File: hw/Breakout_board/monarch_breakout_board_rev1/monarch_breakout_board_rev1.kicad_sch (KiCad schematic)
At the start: 21 parts, among them U2 FDC2214RGHR, U3 INA226AQDGSRQ1, U4 INA226AQDGSRQ1

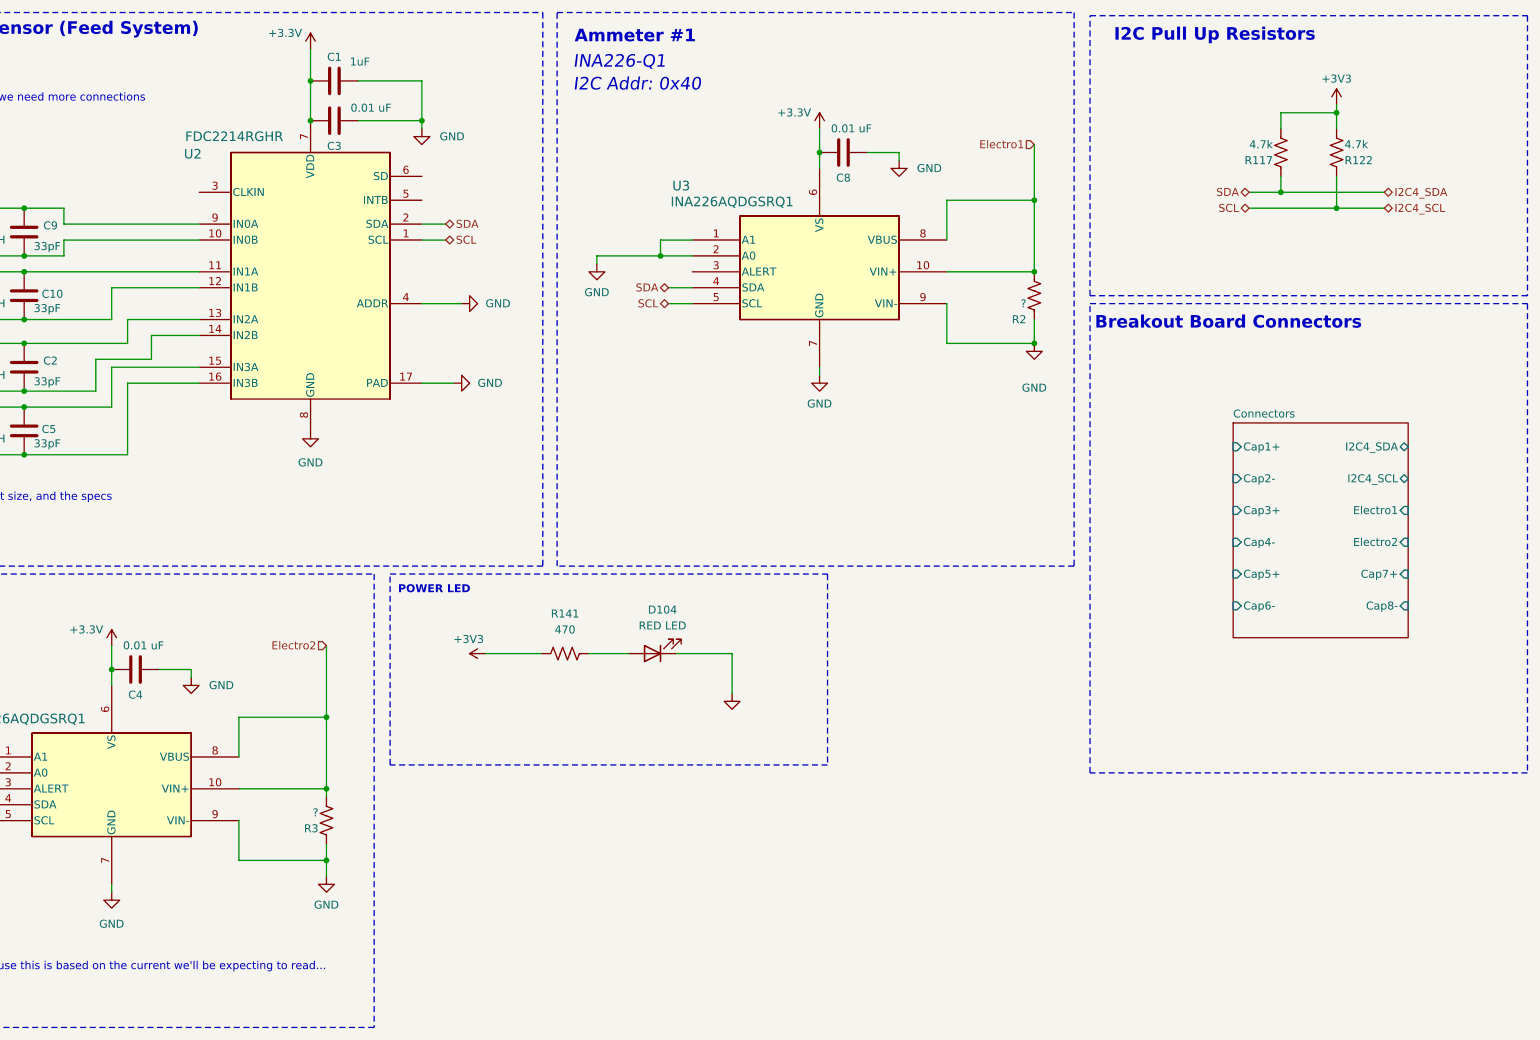
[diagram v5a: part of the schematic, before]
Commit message: 40 Mhz Clock Work + Test Software for Main Control Flow on Dev Board
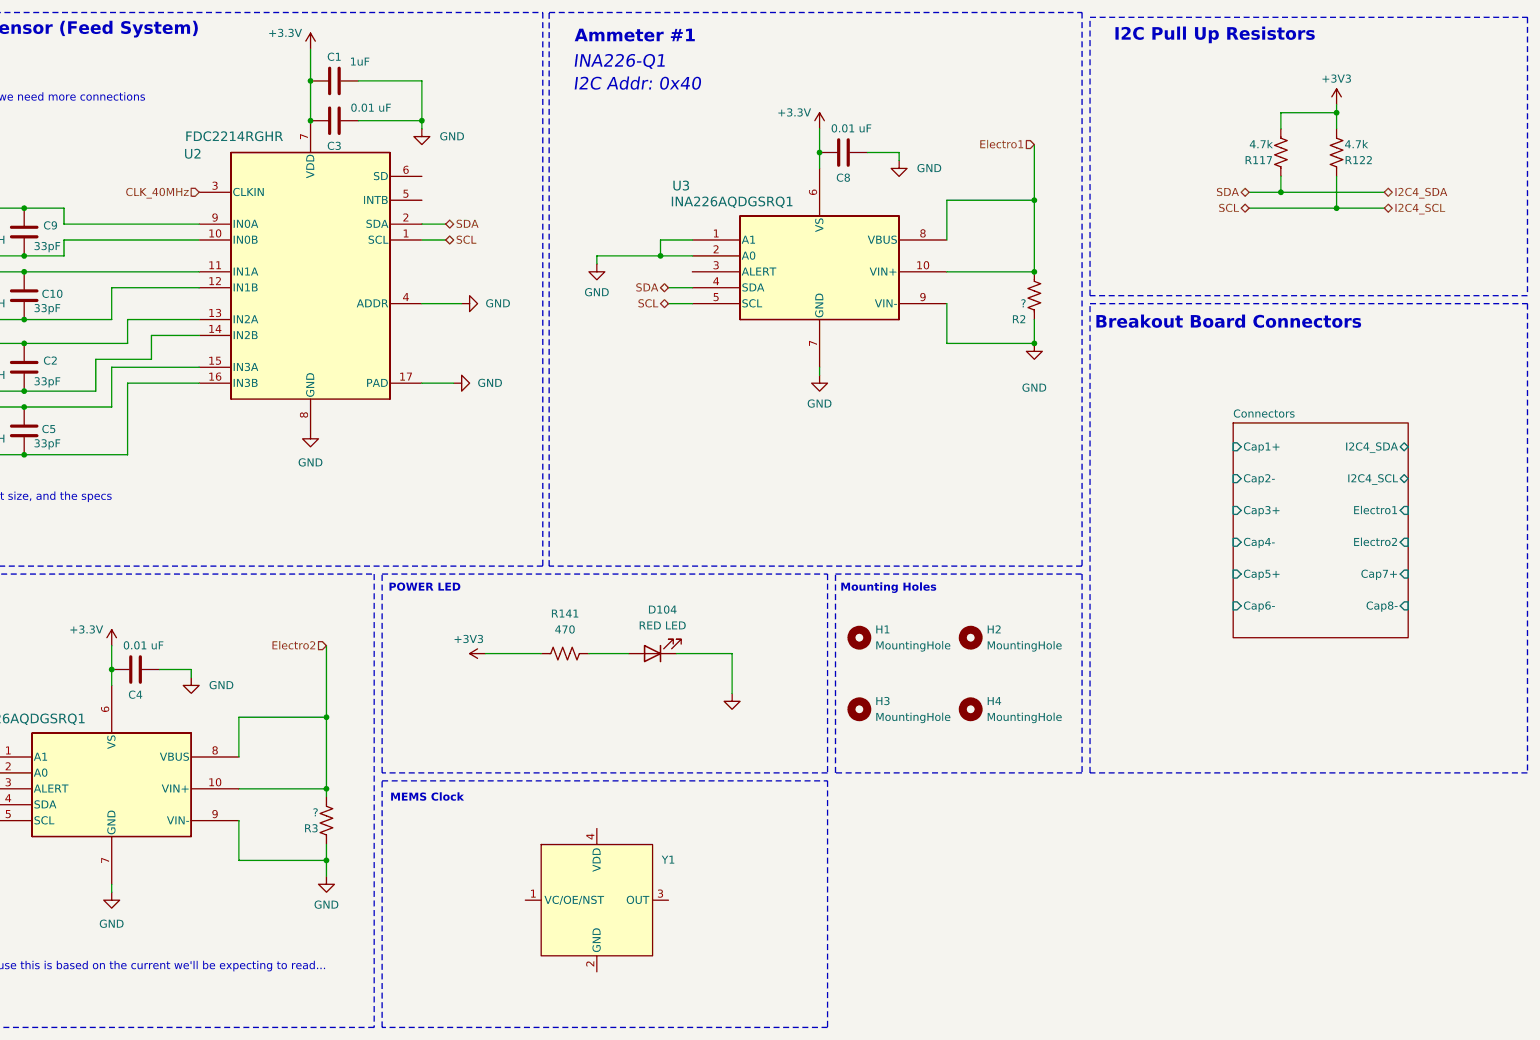
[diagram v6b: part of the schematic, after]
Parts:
- added H1, H2, H3, H4: MountingHole, symbol Mechanical:MountingHole
- added Y1: ~, symbol SIT5000AI-2E-33N0-40.000000X:SIT5000_1
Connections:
- net CLK_40MHz: now reaches U2.3 (CLKIN)
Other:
- note added: "MEMS Clock"
- note added: "Mounting Holes"

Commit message: Breakout Board History Fix
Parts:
- H1, H2, H3, H4: footprint (none) -> MountingHole:MountingHole_2.2mm_M2_DIN965_Pad
- Y1: value ~ -> SiT5000AI-2E-33N0-40; footprint (none) -> Oscillator:Oscillator_SMD_SiT_PQFN-4Pin_3.2x2.5mm
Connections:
- net +3.3V: now also Y1.4 (VDD)
- net CLK_40MHz: now also Y1.3 (OUT)
- net GND: now also Y1.2 (GND)
- no-connect marks 0 -> 4
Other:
- sheet Connectors ports: added none; removed Cap1+, Cap2-, Cap3+, Cap4-, Cap5+, Cap6-, Cap7+, Cap8-, Electro1, Electro2, I2C4_SCL, I2C4_SDA
- note added: "MEMS Clock 40 MHz"
- note added: "What resistor should we use this is based on the current we'll be expecting to read... or amplifier circuit"
- note removed: "MEMS Clock"
- note removed: "Need to look into the exact inductors needed, the footprint size, and the specs"
- note removed: "What does this alert do"
- note removed: "What resistor should we use this is based on the current we'll be expecting to read..."

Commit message: Revert "Crystal Clock Completion, All Pins Assigned, More Routing Work"
This reverts commit 432819c756e1f3cf9abb2627b488983cb7a3cfe3
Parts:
- H1, H2, H3, H4: footprint MountingHole:MountingHole_2.2mm_M2_DIN965_Pad -> (none)
- Y1: value SiT5000AI-2E-33N0-40 -> ~; footprint Oscillator:Oscillator_SMD_SiT_PQFN-4Pin_3.2x2.5mm -> (none)
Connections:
- net +3.3V: no longer Y1.4 (VDD)
- net CLK_40MHz: no longer Y1.3 (OUT)
- net GND: no longer Y1.2 (GND)
- no-connect marks 4 -> 0
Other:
- sheet Connectors ports: added Cap1+, Cap2-, Cap3+, Cap4-, Cap5+, Cap6-, Cap7+, Cap8-, Electro1, Electro2, I2C4_SCL, I2C4_SDA; removed none
- note added: "MEMS Clock"
- note added: "Need to look into the exact inductors needed, the footprint size, and the specs"
- note added: "What does this alert do"
- note added: "What resistor should we use this is based on the current we'll be expecting to read..."
- note removed: "MEMS Clock 40 MHz"
- note removed: "What resistor should we use this is based on the current we'll be expecting to read... or amplifier circuit"
